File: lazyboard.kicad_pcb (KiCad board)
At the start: 2 copper layers, 30.5 x 40.6 mm, 15 parts, among them J1 QWIIC/STEMMA, J2 Conn_01x06_Pin, J3 Conn_01x06_Pin, J4 Conn_01x03_Pin, J5 Conn_01x06_Pin, J6 Conn_01x06_Pin, P1 USB_C_Plug_USB2.0, SW1 SW_Push, SW2 SW_Push, U2 AP2112K-3.3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

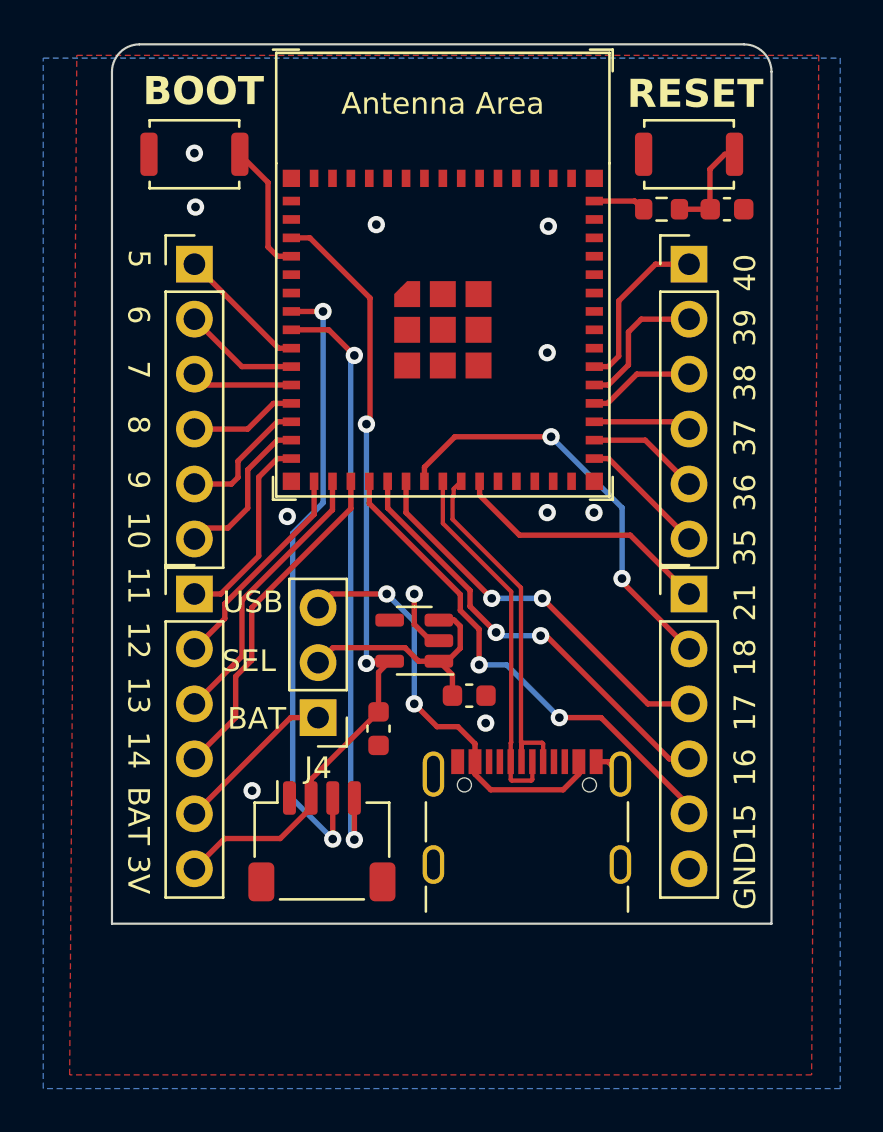
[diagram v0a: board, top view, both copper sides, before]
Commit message: fixed reset bug
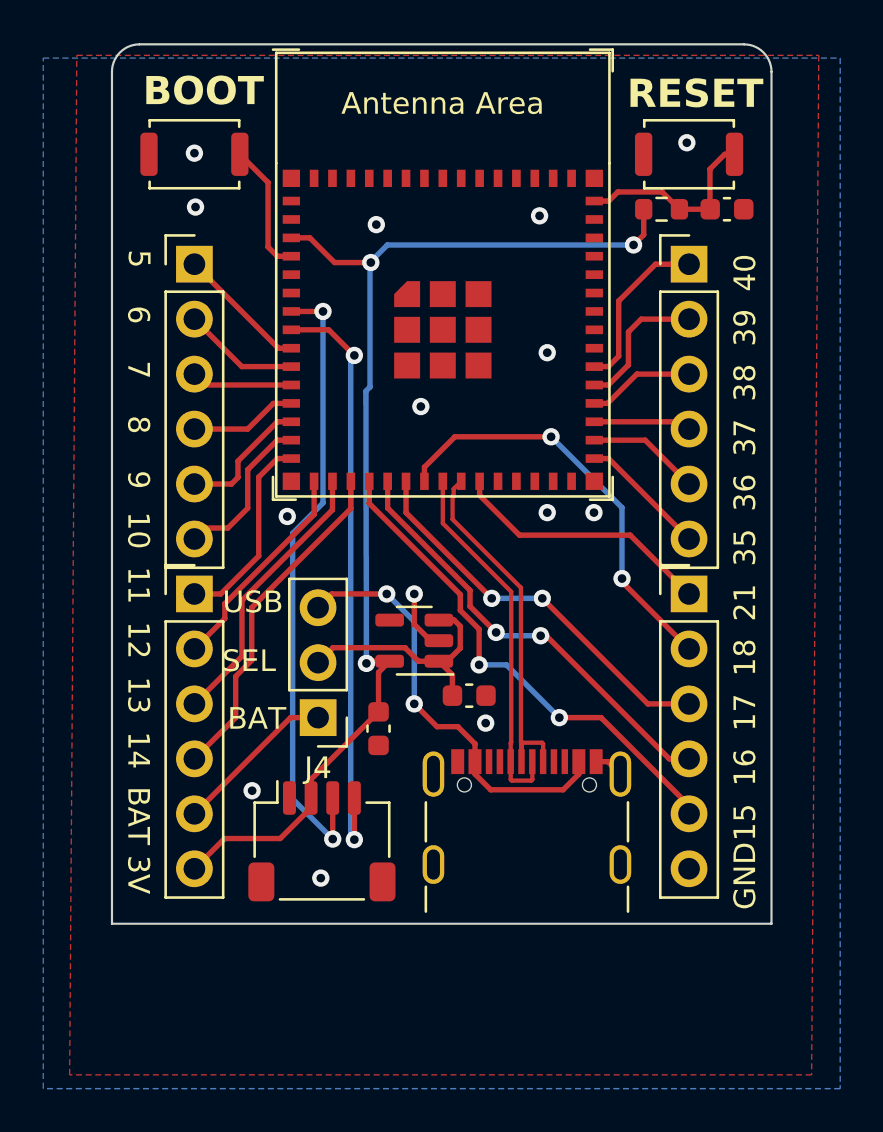
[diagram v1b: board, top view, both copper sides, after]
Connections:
- C1 pad 1: Net-(C1-Pad1) -> RESET
- R1 pad 1: RESET -> +3.3V
- R1 pad 2: Net-(C1-Pad1) -> RESET
- SW1 pad 1: Net-(C1-Pad1) -> RESET
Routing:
- net +3.3V: track 37.8 -> 53.2 mm, vias 2 -> 3
- net RESET: track 2.44 -> 9.14 mm
- net Net-(C1-Pad1): track 4.70 -> 0.00 mm
- net GND: vias 11 -> 14
